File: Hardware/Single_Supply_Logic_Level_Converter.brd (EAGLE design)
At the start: 25.4 x 26 mm, 23 parts, among them U1 TXB0104, U2 TPS61200, U4 MIC5219-3.3

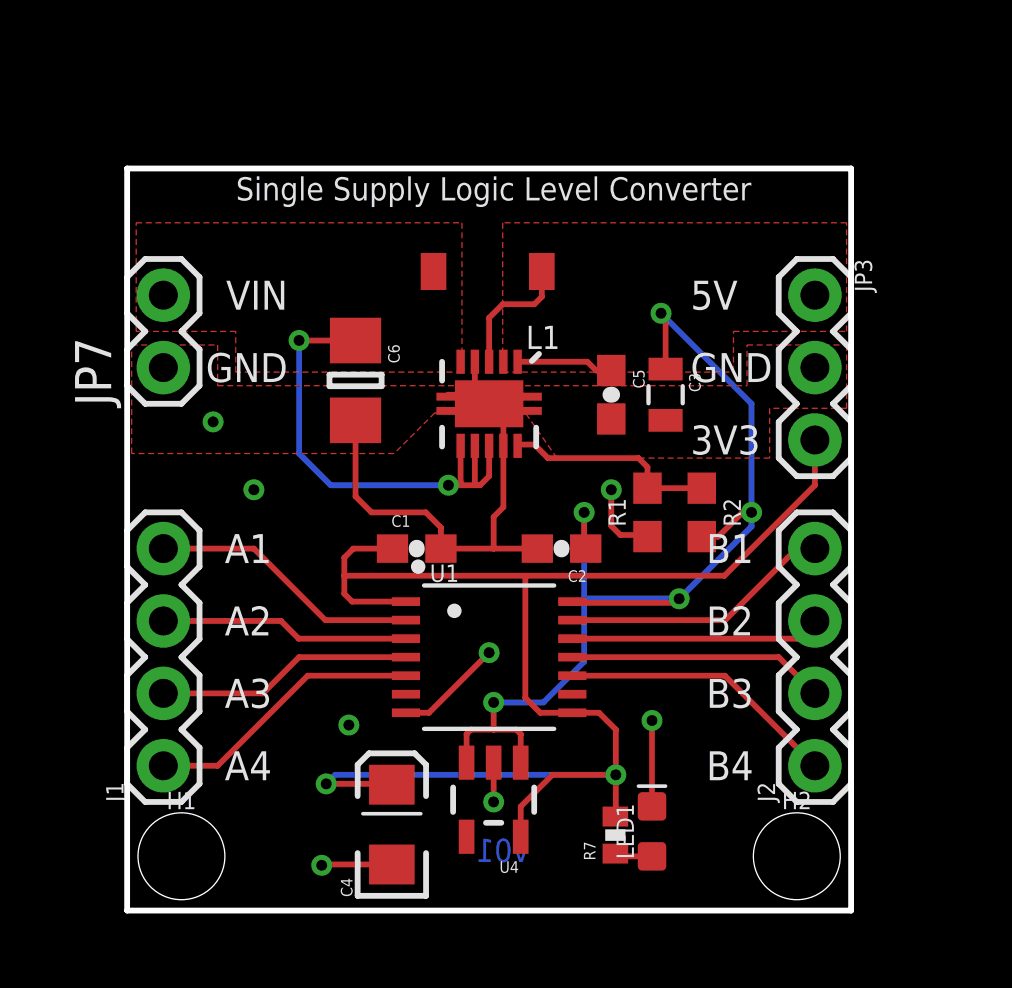
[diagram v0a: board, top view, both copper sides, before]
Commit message: Vout voltage from Vreg directly
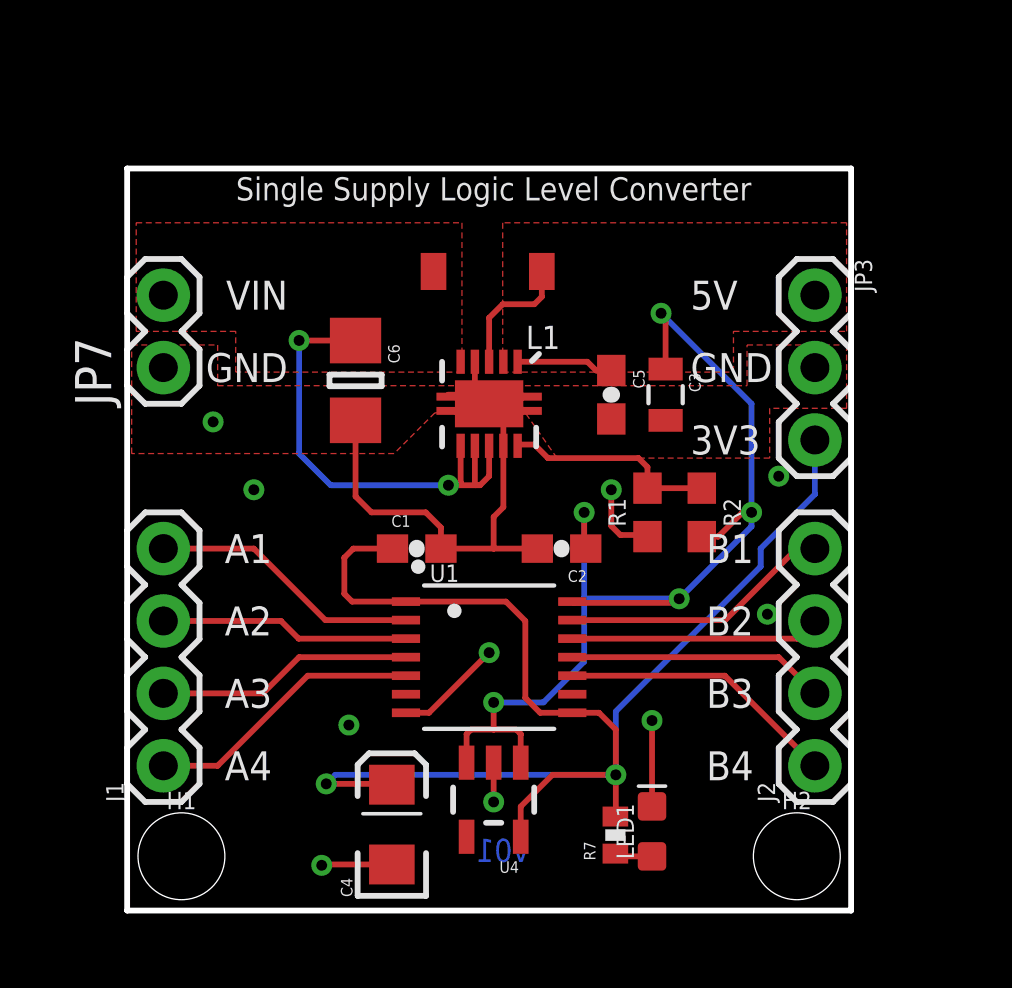
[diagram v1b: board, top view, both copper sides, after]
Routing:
- net 3.3V: track 53.2 -> 51.3 mm
- net GND: vias 8 -> 10
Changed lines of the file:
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@@
 <wire x1="9.31" y1="12.7" x2="7.9375" y2="12.7" width="0.2032" layer="1"/>
 <wire x1="7.62" y1="12.3825" x2="7.9375" y2="12.7" width="0.2032" layer="1"/>
-<wire x1="24.13" y1="16.51" x2="24.13" y2="14.9225" width="0.2032" layer="1"/>
-<wire x1="24.13" y1="14.9225" x2="20.955" y2="11.7475" width="0.2032" layer="1"/>
 <wire x1="15.6178" y1="6.94" x2="14.49125" y2="6.94" width="0.2032" layer="1"/>
-<wire x1="14.49125" y1="6.94" x2="13.97" y2="7.46125" width="0.2032" layer="1"/>
+<wire x1="13.97" y1="7.46125" x2="14.49125" y2="6.94" width="0.2032" layer="1"/>
 <wire x1="15.6178" y1="6.94" x2="16.555" y2="6.94" width="0.2032" layer="1"/>
 <wire x1="16.555" y1="6.94" x2="17.145" y2="6.35" width="0.2032" layer="1"/>
@@
 <wire x1="7.8925" y1="10.84" x2="7.62" y2="11.1125" width="0.2032" layer="1"/>
 <wire x1="9.7822" y1="10.84" x2="7.8925" y2="10.84" width="0.2032" layer="1"/>
-<wire x1="7.62" y1="11.1125" x2="7.62" y2="11.7475" width="0.2032" layer="1"/>
-<wire x1="7.62" y1="11.7475" x2="7.62" y2="12.3825" width="0.2032" layer="1"/>
-<wire x1="20.955" y1="11.7475" x2="13.97" y2="11.7475" width="0.2032" layer="1"/>
-<wire x1="13.97" y1="11.7475" x2="7.62" y2="11.7475" width="0.2032" layer="1"/>
-<wire x1="13.97" y1="7.46125" x2="13.97" y2="11.7475" width="0.2032" layer="1"/>
+<wire x1="7.62" y1="11.1125" x2="7.62" y2="12.3825" width="0.2032" layer="1"/>
+<wire x1="9.7822" y1="10.84" x2="13.29" y2="10.84" width="0.2032" layer="1"/>
+<wire x1="13.29" y1="10.84" x2="13.97" y2="10.16" width="0.2032" layer="1"/>
+<wire x1="13.97" y1="10.16" x2="13.97" y2="7.46125" width="0.2032" layer="1"/>
+<wire x1="24.13" y1="16.51" x2="24.13" y2="14.605" width="0.2032" layer="16"/>
+<wire x1="24.13" y1="14.605" x2="22.225" y2="12.7" width="0.2032" layer="16"/>
+<wire x1="17.145" y1="4.7625" x2="17.145" y2="6.985" width="0.2032" layer="16"/>
+<wire x1="17.145" y1="6.985" x2="22.225" y2="12.065" width="0.2032" layer="16"/>
+<wire x1="22.225" y1="12.065" x2="22.225" y2="12.7" width="0.2032" layer="16"/>
 </signal>
 <signal name="5V">
@@
 <wire x1="16.98625" y1="13.49375" x2="16.98625" y2="14.76375" width="0.2032" layer="1"/>
 <wire x1="18.2" y1="13.17625" x2="17.30375" y2="13.17625" width="0.2032" layer="1"/>
+<via x="22.86" y="15.24" extent="1-16" drill="0.381"/>
+<via x="22.463125" y="10.398125" extent="1-16" drill="0.381"/>
 </signal>
 <signal name="A4">

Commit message: resizing board to 1x1 inch
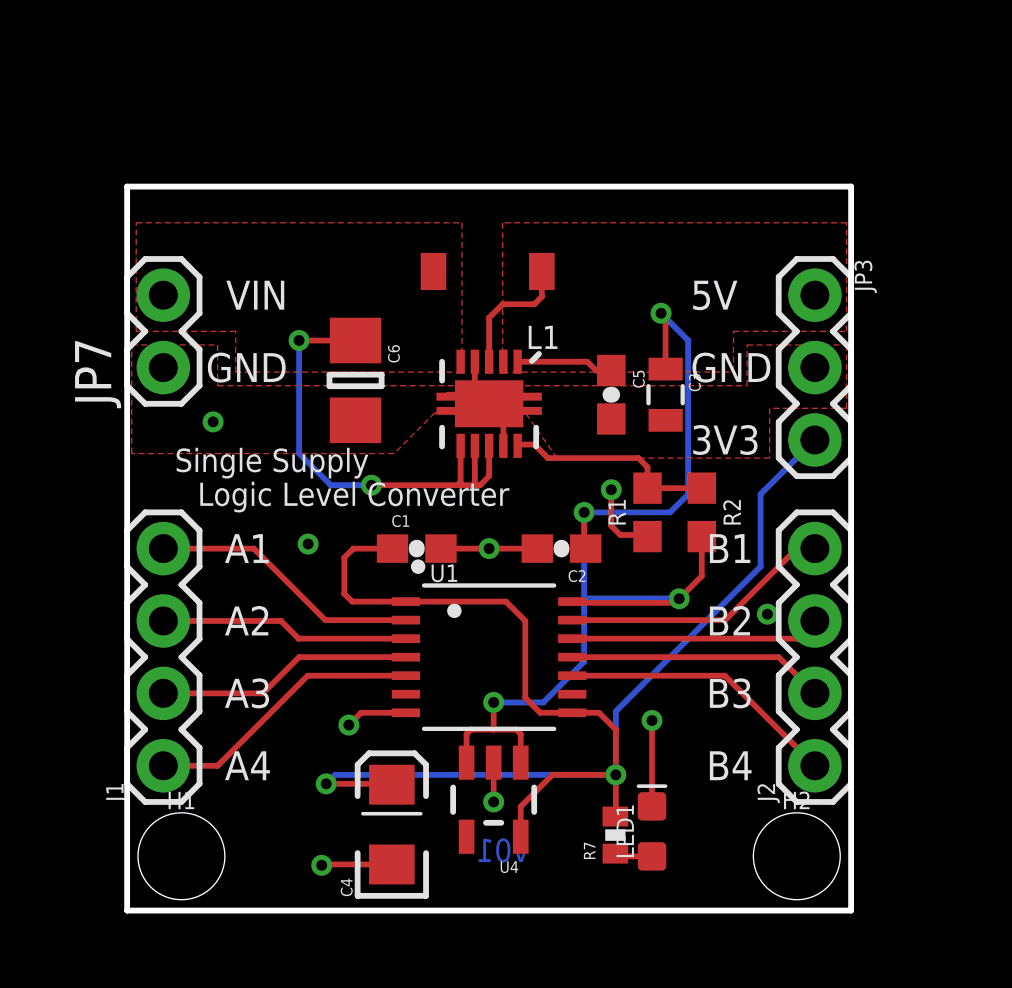
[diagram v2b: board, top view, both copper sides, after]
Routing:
- net GND: track 33.5 -> 21.3 mm, vias 10 -> 9
- net 5V: track 39.0 -> 37.7 mm, vias 5 -> 4
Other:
- board size 25.4 x 26 mm -> 25.4 x 25.4 mm
- board text added: "Logic Level Converter"
- board text added: "Single Supply"

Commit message: Adding top ground plane
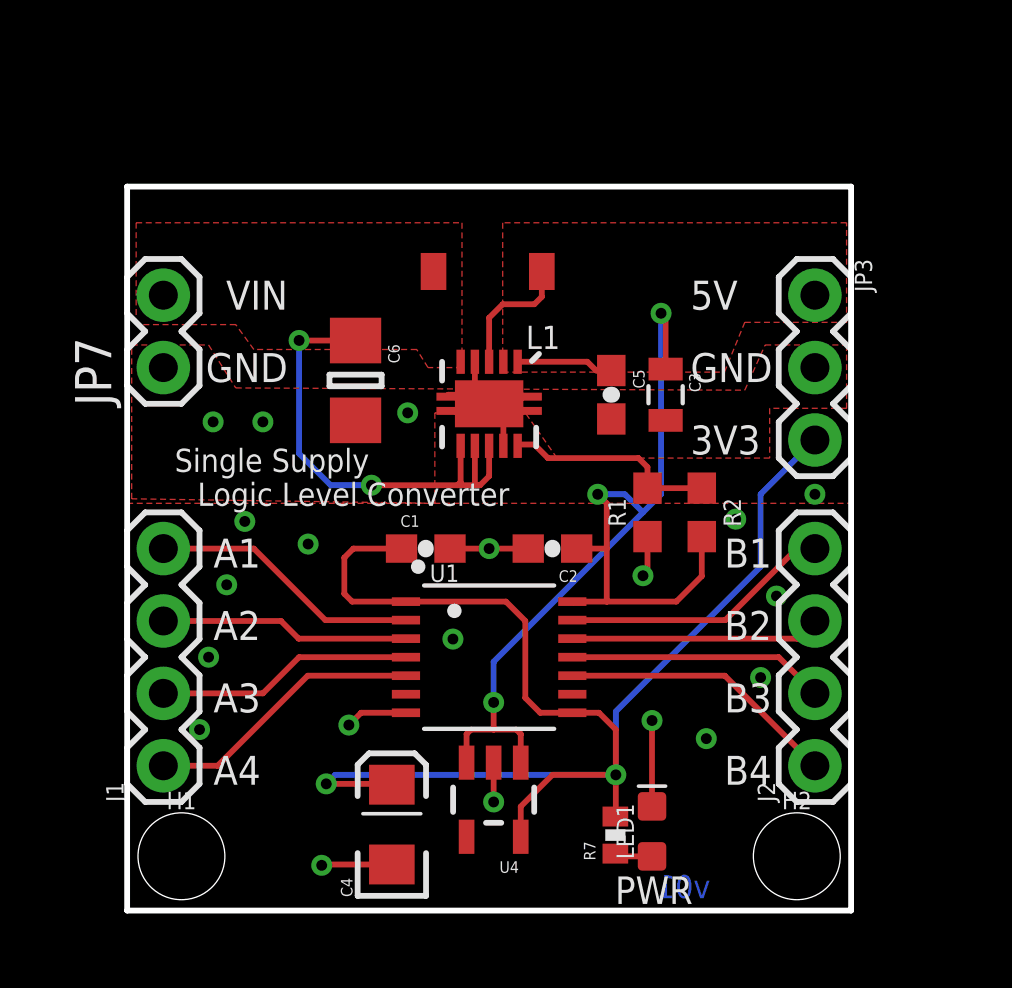
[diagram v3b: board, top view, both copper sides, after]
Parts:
- moved C2 0.32 mm to (14.9, 12.7)
- moved C1 0.32 mm to (10.5, 12.7)
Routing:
- net GND: track 21.3 -> 19.4 mm, vias 9 -> 18
- net 5V: track 37.7 -> 36.3 mm, vias 4 -> 3
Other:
- board text added: "PWR"

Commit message: Updating design per review
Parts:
- removed H1, H2: STAND-OFFTIGHT, SparkFun-Hardware:STAND-OFF-TIGHT
- removed LED1: RED, SparkFun-LED:LED-0603
- removed R7: 1K, SparkFun:0402-RES
- removed U4: MIC5219-3.3, SparkFun:SOT23-5
- added C7: 10uF, SparkFun-Capacitors:EIA3216
- added D1: RED, SparkFun-LED:LED-0603
- added FD1, FD2, FD3, FD4: FIDUCIALUFIDUCIAL, SparkFun-Aesthetics:FIDUCIAL-MICRO
- added J3, J4: (no value), SparkFun-Connectors:1X01
- added JP1: JUMPER-SMT_3_1-NC_TRACE_SILK, SparkFun-Jumpers:SMT-JUMPER_3_1-NC_TRACE_SILK
- added JP2: JUMPER-SMT_2_NC_TRACE_SILK, SparkFun-Jumpers:SMT-JUMPER_2_NC_TRACE_SILK
- added LOGO3: SFE_LOGO_FLAME.1_INCH, SparkFun-Aesthetics:SFE_LOGO_FLAME_.1
- added LOGO4: OSHW-LOGOS, SparkFun-Aesthetics:OSHW-LOGO-S
- added R3: 1k, SparkFun-Resistors:0603
- added R4: 13k, SparkFun-Resistors:0603
- added R5: 22k, SparkFun-Resistors:0603
- added R6: (no value), SparkFun-Resistors:AXIAL-0.3
- added U$10, U$38: (no value), Single_Supply_Logic_Level_Converter_Lables:A16
- added U$11, U$39: (no value), Single_Supply_Logic_Level_Converter_Lables:A27
- added U$12, U$40: (no value), Single_Supply_Logic_Level_Converter_Lables:A38
- added U$13, U$41: (no value), Single_Supply_Logic_Level_Converter_Lables:A49
- added U$14, U$46: (no value), Single_Supply_Logic_Level_Converter_Lables:B110
- added U$15, U$45: (no value), Single_Supply_Logic_Level_Converter_Lables:B211
- added U$16, U$43: (no value), Single_Supply_Logic_Level_Converter_Lables:B312
- added U$17, U$42: (no value), Single_Supply_Logic_Level_Converter_Lables:B413
- added U$18, U$36: (no value), Single_Supply_Logic_Level_Converter_Lables:CONVERTER19
- added U$19, U$26, U$30, U$31, U$32, U$33, U$37, U$47, U$48, U$50: (no value), Single_Supply_Logic_Level_Converter_Lables:GND0
- added U$20: (no value), Single_Supply_Logic_Level_Converter_Lables:JP114
- added U$21: (no value), Single_Supply_Logic_Level_Converter_Lables:JP215
- added U$22, U$35: (no value), Single_Supply_Logic_Level_Converter_Lables:LOGIC__LEVEL18
- added U$23, U$44: (no value), Single_Supply_Logic_Level_Converter_Lables:RPTH16
- added U$24, U$53: (no value), Single_Supply_Logic_Level_Converter_Lables:SINGLE_SUPPLY17
- added U$25, U$29: (no value), voltageIn:1#5#5V0
- added U$27, U$8: (no value), Single_Supply_Logic_Level_Converter_Lables:VIN1
- added U$28, U$52: (no value), Single_Supply_Logic_Level_Converter_Lables:VOUT2
- added U$49, U$7: (no value), Single_Supply_Logic_Level_Converter_Lables:3#3V20
- added U$51, U$9: (no value), Single_Supply_Logic_Level_Converter_Lables:5V3
- added U3: ADJ, SparkFun-IC-Power:SOT23-5
- C4: value 10uF -> 470pF; device SparkFun:EIA3216 -> SparkFun-Capacitors:0603
- C5: device SparkFun:0603-CAP -> SparkFun-Capacitors:0603
- C6: device CH_passive:1206 -> SparkFun-Capacitors:0603
- JP3: device SparkFun-Connectors:1X03 -> SparkFun-Connectors:1X04
- U2: device SparkFun:QFN-10_PAD -> SparkFun-IC-Power:QFN-10_PAD
- moved C4 9.09 mm to (17.5, 6.99), turned to 270 degrees
- moved R1 5.11 mm to (16.0, 18.6), turned to 0 degrees
- moved C6 5.07 mm to (11.3, 22.5)
- moved R2 4.67 mm to (19.4, 18.6), turned to 0 degrees
- moved JP3 4.58 mm to (26.7, 25.4)
- moved L1 4.33 mm to (12.0, 26.7)
- moved C2 4.13 mm to (16.5, 16.5)
- moved C3 4.13 mm to (18.9, 22.2)
- moved C1 4.02 mm to (11.7, 16.5)
- moved U1 4.02 mm to (14.0, 12.7)
- moved U2 4.02 mm to (14.0, 21.6)
- moved JP7 3.81 mm to (1.27, 22.9)
- moved C5 3.51 mm to (16.7, 21.6)
- moved J2 2.54 mm to (26.7, 5.08)
- moved FRAME1 2.25 mm to (-4.95, -10.2)
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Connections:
- removed net 3.3V: C1.1, C4.A, JP3.3, R7.2, U1.1, U1.8, U4.5
- removed net N$4: LED1.A, R7.1
- new net N$1: JP1.3, U3.5
- new net N$11: C4.1, R4.1, R5.2, R6.P$1, U3.4
- new net N$12: JP2.1, R4.2
- new net N$3: D1.A, R3.1
- new net VCCA: C1.1, C7.+, JP1.1, JP1.2, JP2.2, JP3.3, R3.2, R6.P$2, U1.1, U1.8
- net 5V: now also U3.1, U3.3; no longer U4.1, U4.3
- net GND: now also C4.2, C7.-, D1.C, J3.1, J4.1, JP3.4, R5.1, U3.2; no longer C4.C, LED1.C, U4.2
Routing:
- net VCCA: track 0.00 -> 76.6 mm, vias 0 -> 3
- net 3.3V: track 51.6 -> 0.00 mm, vias 2 -> 0
- net N$11: track 0.00 -> 28.8 mm
- net N$1: track 0.00 -> 9.14 mm
- net GND: track 19.4 -> 11.8 mm, vias 18 -> 17
- net N$12: track 0.00 -> 4.08 mm
- net B4: track 9.82 -> 12.7 mm
- net B3: track 9.04 -> 11.9 mm
- net A4: track 9.82 -> 12.7 mm
- net A3: track 9.04 -> 11.9 mm
- net B2: track 8.77 -> 11.1 mm
- net A2: track 8.77 -> 11.1 mm
- net 5V: track 36.3 -> 38.3 mm, vias 3 -> 4
- net FB: track 7.55 -> 5.89 mm
- net N$3: track 0.00 -> 1.65 mm
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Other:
- board size 25.4 x 25.4 mm -> 27.9 x 29.8 mm
- board text added: "All Units in Inches"
- board text added: "Mary West"
- board text removed: "3V3"
- board text removed: "5V"
- board text removed: "A1"
- board text removed: "A2"
- board text removed: "A3"
- board text removed: "A4"
- board text removed: "B1"
- board text removed: "B2"
- board text removed: "B3"
- board text removed: "B4"
- board text removed: "GND"
- board text removed: "Logic Level Converter"
- board text removed: "PWR"
- board text removed: "Single Supply"
- board text removed: "Single Supply Logic Level Converter"
- board text removed: "VCCA: 3.3V"
- board text removed: "VIN"
- board text removed: "VOUT"

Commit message: New labels
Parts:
- U$25, U$29: device voltageIn:1#5#5V0 -> voltageIn:3#5V0
- moved JP2 14.0 mm to (7.14, 3.17)
- moved U$21 14.0 mm to (5.40, 1.11)
- moved JP1 13.3 mm to (20.6, 3.17)
- moved U$20 13.3 mm to (18.9, 1.11)
- moved D1 12.7 mm to (20.3, 6.99)
- moved R4 11.4 mm to (7.78, 6.99)
- moved R3 9.84 mm to (19.0, 6.99)
- moved C4 7.94 mm to (9.53, 6.99)
- moved U$25 6.11 mm to (2.78, 25.6), flipped to the top
- moved C7 5.40 mm to (16.7, 6.99)
- moved FD1 5.24 mm to (21.6, 27.9)
- moved FD2 5.24 mm to (21.6, 27.9)
- moved U$29 5.08 mm to (7.94, 25.6), flipped to the bottom
- moved U3 2.25 mm to (12.7, 6.99), turned to 180 degrees
- moved R5 0.63 mm to (14.0, 2.94)
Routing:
- net N$11: track 28.8 -> 21.1 mm
- net N$1: track 9.14 -> 13.9 mm, vias 0 -> 2
- net VCCA: track 76.6 -> 72.9 mm
- net N$3: track 1.65 -> 0.00 mm
- net N$12: track 4.08 -> 3.48 mm
- net 5V: track 38.3 -> 38.6 mm, vias 4 -> 3
- net GND: vias 17 -> 18
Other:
- board size 27.9 x 29.8 mm -> 27.9 x 29.2 mm
- board text removed: "VCCB: 5V"
